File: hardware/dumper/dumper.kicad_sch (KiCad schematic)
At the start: 21 parts, among them J1 /Reset, J10 arduino 10, J11 ss, J2 Clock In, J3 data, J4 clock, J5 2816 /WR disconnect, J6 arduino 13, J7 arduino 11, J8 arduino 5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

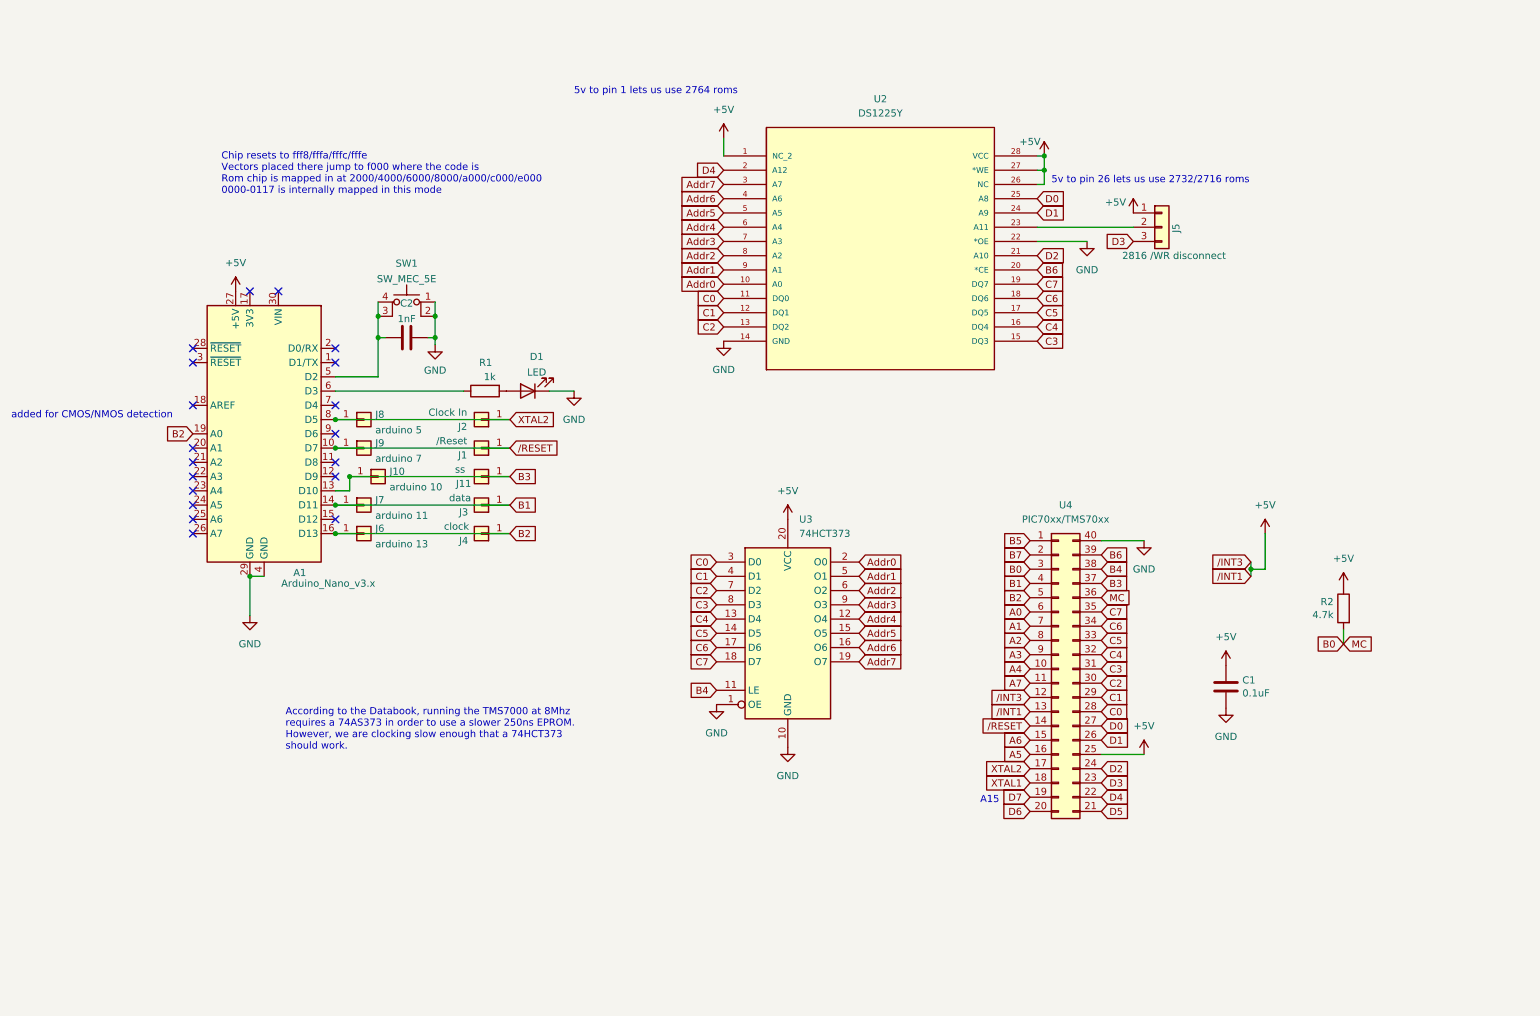
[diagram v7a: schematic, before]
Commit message: Update dumper to memory-mapped I/O version
TBD extra port detection pins
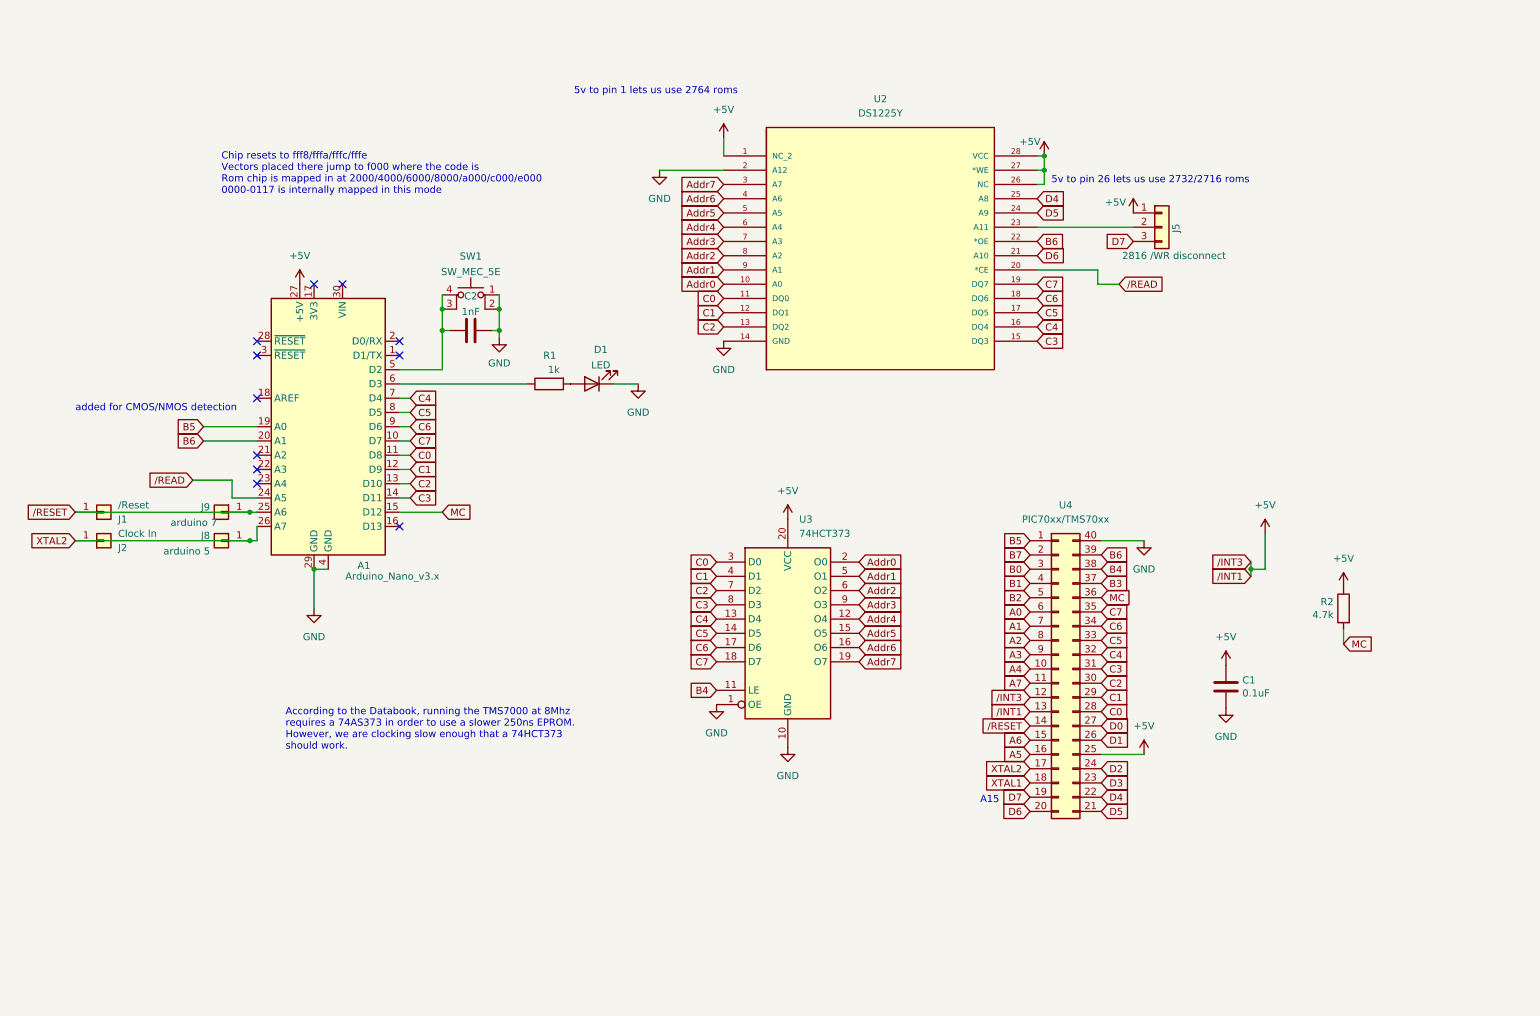
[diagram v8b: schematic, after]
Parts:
- removed J10: arduino 10, Connector_PinHeader_2.54mm:PinHeader_1x01_P2.54mm_Vertical, symbol Connector_Generic:Conn_01x01
- removed J11: ss, Connector_PinHeader_2.54mm:PinHeader_1x01_P2.54mm_Vertical, symbol Connector_Generic:Conn_01x01
- removed J3: data, Connector_PinHeader_2.54mm:PinHeader_1x01_P2.54mm_Vertical, symbol Connector_Generic:Conn_01x01
- removed J4: clock, Connector_PinHeader_2.54mm:PinHeader_1x01_P2.54mm_Vertical, symbol Connector_Generic:Conn_01x01
- removed J6: arduino 13, Connector_PinHeader_2.54mm:PinHeader_1x01_P2.54mm_Vertical, symbol Connector_Generic:Conn_01x01
- removed J7: arduino 11, Connector_PinHeader_2.54mm:PinHeader_1x01_P2.54mm_Vertical, symbol Connector_Generic:Conn_01x01
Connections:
- net B0: no longer R2.2, U4.36 (Pin_36)
- net B1: no longer A1.14 (D11)
- net B2: no longer A1.16 (D13), A1.19 (A0)
- net B3: no longer A1.13 (D10)
- net B5: now also A1.19 (A0)
- net B6: now also A1.20 (A1), U2.22 (*OE); no longer U2.20 (*CE)
- net C0: now also A1.11 (D8)
- net C1: now also A1.12 (D9)
- net C2: now also A1.13 (D10)
- net C3: now also A1.14 (D11)
- net C4: now also A1.7 (D4)
- net C5: now also A1.8 (D5)
- net C6: now also A1.9 (D6)
- net C7: now also A1.10 (D7)
- net D0: no longer U2.25 (A8)
- net D1: no longer U2.24 (A9)
- net D2: no longer U2.21 (A10)
- net D3: no longer J5.3 (Pin_3)
- net D4: now also U2.25 (A8); no longer U2.2 (A12)
- net D5: now also U2.24 (A9)
- net D6: now also U2.21 (A10)
- net D7: now also J5.3 (Pin_3)
- net GND: now also U2.2 (A12); no longer U2.22 (*OE)
- net XTAL2: now also A1.26 (A7); no longer A1.8 (D5)
- net /RESET: now also A1.25 (A6); no longer A1.10 (D7)
- net MC: now reaches A1.15 (D12)
- net MC: now also R2.2, U4.36 (Pin_36)
- net /READ: now reaches A1.24 (A5)
- net /READ: now also U2.20 (*CE)
- no-connect marks 19 -> 11
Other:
- moved on the sheet: A1, C2, D1, J1, J2, J8, J9, R1, SW1
